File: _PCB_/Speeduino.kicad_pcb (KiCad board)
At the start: 2 copper layers, 100 x 100 mm, 13 parts, among them U1 TC4424AVOA, U2 TC4424AVOA

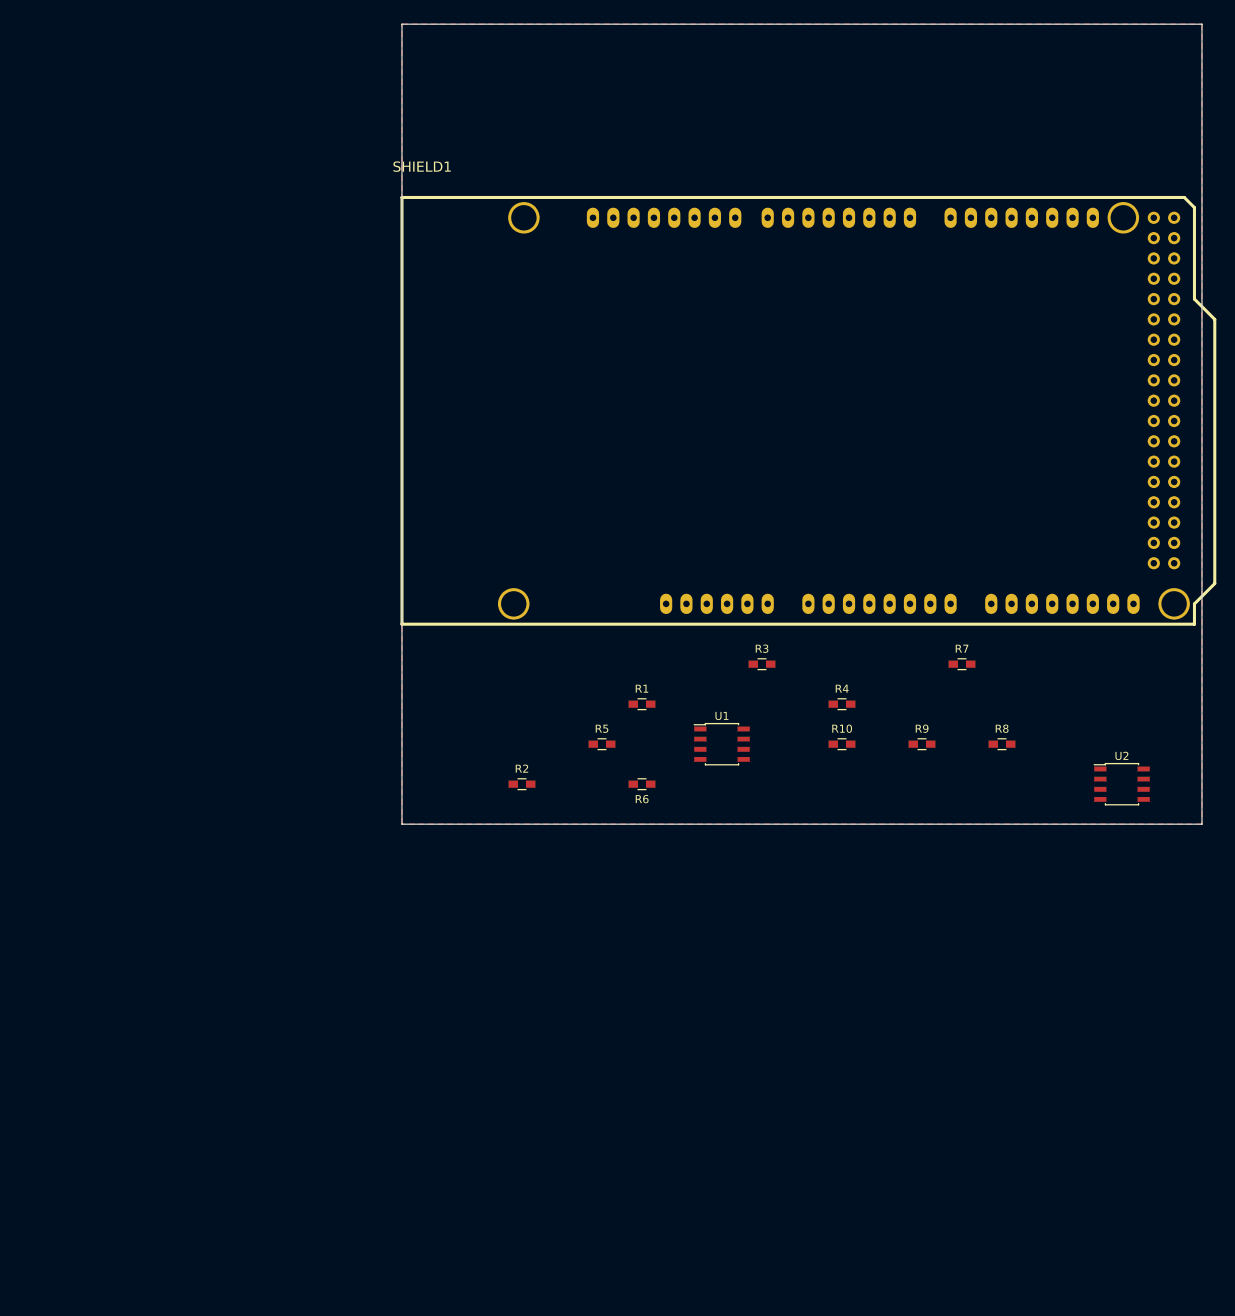
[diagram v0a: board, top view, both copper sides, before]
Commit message: - ajout schematic 4 injecteurs
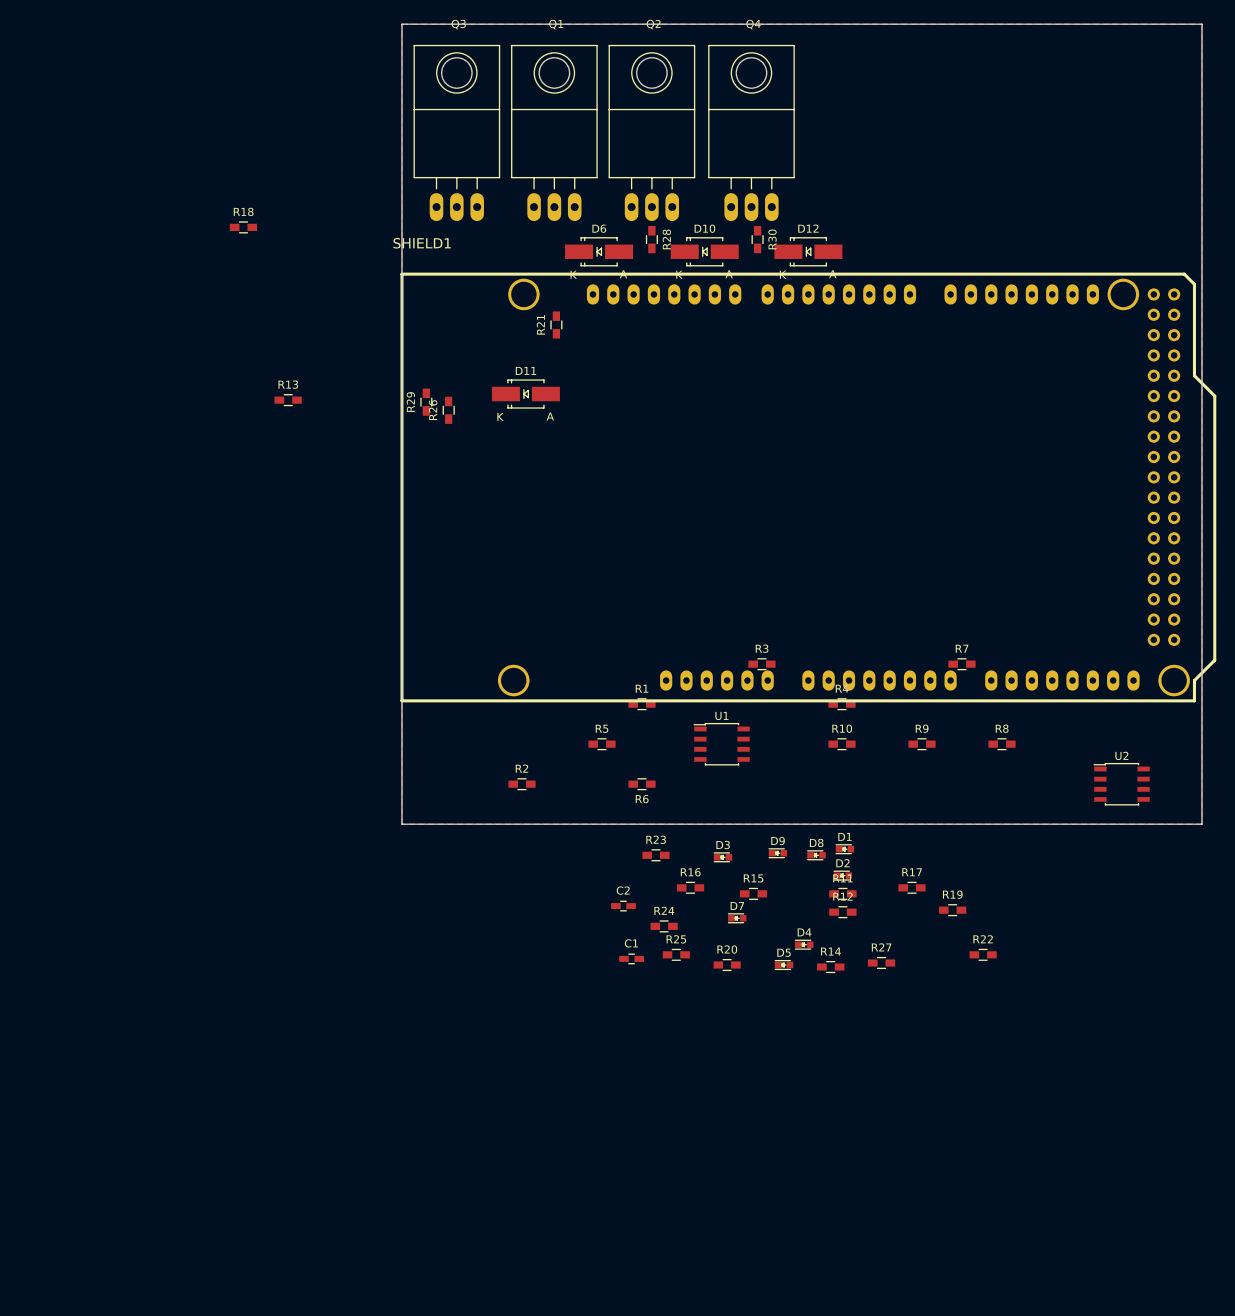
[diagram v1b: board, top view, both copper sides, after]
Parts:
- added C1: C, Speeduino:C_0603_HandSoldering, F.Cu at (108.7, 146.8)
- added C2: C, Speeduino:C_0603_HandSoldering, F.Cu at (107.7, 140.2)
- added D1: LED, Speeduino:LED_0603, F.Cu at (135.4, 133.1)
- added D10: D, Speeduino:SMA_Handsoldering, F.Cu at (117.8, 58.4)
- added D11: D, Speeduino:SMA_Handsoldering, F.Cu at (95.5, 76.2)
- added D12: D, Speeduino:SMA_Handsoldering, F.Cu at (130.8, 58.4)
- added D2: LED, Speeduino:LED_0603, F.Cu at (135.1, 136.4)
- added D3: LED, Speeduino:LED_0603, F.Cu at (120.1, 134.1)
- added D4: LED, Speeduino:LED_0603, F.Cu at (130.3, 145.1)
- added D5: LED, Speeduino:LED_0603, F.Cu at (127.8, 147.6)
- added D6: D, Speeduino:SMA_Handsoldering, F.Cu at (104.6, 58.4)
- added D7: LED, Speeduino:LED_0603, F.Cu at (121.9, 141.8)
- added D8: LED, Speeduino:LED_0603, F.Cu at (131.8, 133.9)
- added D9: LED, Speeduino:LED_0603, F.Cu at (127.0, 133.6)
- added Q1: STP62NS04Z, Speeduino:TO-220_Neutral123_Horizontal_LargePads, F.Cu at (99.0, 52.9)
- added Q2: STP62NS04Z, Speeduino:TO-220_Neutral123_Horizontal_LargePads, F.Cu at (111.2, 52.9)
- added Q3: STP62NS04Z, Speeduino:TO-220_Neutral123_Horizontal_LargePads, F.Cu at (86.9, 52.9)
- added Q4: STP62NS04Z, Speeduino:TO-220_Neutral123_Horizontal_LargePads, F.Cu at (123.7, 52.9)
- added R11: R, Speeduino:R_0603_HandSoldering, F.Cu at (135.1, 138.7)
- added R12: R, Speeduino:R_0603_HandSoldering, F.Cu at (135.1, 141.0)
- added R13: R, Speeduino:R_0603_HandSoldering, F.Cu at (65.8, 77.0)
- added R14: R, Speeduino:R_0603_HandSoldering, F.Cu at (133.6, 147.9)
- added R15: R, Speeduino:R_0603_HandSoldering, F.Cu at (123.9, 138.7)
- added R16: R, Speeduino:R_0603_HandSoldering, F.Cu at (116.1, 137.9)
- added R17: R, Speeduino:R_0603_HandSoldering, F.Cu at (143.8, 137.9)
- added R18: R, Speeduino:R_0603_HandSoldering, F.Cu at (60.2, 55.4)
- added R19: 680, Speeduino:R_0603_HandSoldering, F.Cu at (148.8, 140.7)
- added R20: 100K, Speeduino:R_0603_HandSoldering, F.Cu at (120.6, 147.6)
- added R21: 1K, Speeduino:R_0603_HandSoldering, F.Cu at (99.3, 67.6)
- added R22: 680, Speeduino:R_0603_HandSoldering, F.Cu at (152.6, 146.3)
- added R23: 680, Speeduino:R_0603_HandSoldering, F.Cu at (111.8, 133.9)
- added R24: 680, Speeduino:R_0603_HandSoldering, F.Cu at (112.8, 142.8)
- added R25: 100K, Speeduino:R_0603_HandSoldering, F.Cu at (114.3, 146.3)
- added R26: 100K, Speeduino:R_0603_HandSoldering, F.Cu at (85.8, 78.3)
- added R27: 100K, Speeduino:R_0603_HandSoldering, F.Cu at (139.9, 147.3)
- added R28: 1K, Speeduino:R_0603_HandSoldering, F.Cu at (111.2, 56.9)
- added R29: 1K, Speeduino:R_0603_HandSoldering, F.Cu at (83.0, 77.2)
- added R30: 1K, Speeduino:R_0603_HandSoldering, F.Cu at (124.5, 56.9)
- moved SHIELD1 9.58 mm to (80.0, 114.6)
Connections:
- R6 pad 1: (no net) -> +12V
- U1 pad 5: (no net) -> Net-(R11-Pad2)
- U1 pad 7: (no net) -> Net-(R12-Pad2)
- U2 pad 5: (no net) -> Net-(R15-Pad2)
- U2 pad 7: (no net) -> Net-(R16-Pad2)

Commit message: - ajout BSP149
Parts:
- added Q5: BSP149, Speeduino:SOT-223, F.Cu at (150.0, 45.0)
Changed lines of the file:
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@@
 (kicad_pcb (version 4) (host pcbnew 4.0.0-stable)
   (general
-    (links 70)
-    (no_connects 58)
+    (links 71)
+    (no_connects 59)
     (area 79.924999 29.924999 180.075001 130.075001)
     (thickness 1.6)
@@
     (tracks 0)
     (zones 0)
-    (modules 51)
-    (nets 40)
+    (modules 52)
+    (nets 41)
   )
   (page A4)
@@
   (net 38 INJ1-CPU-D8)
   (net 39 INJ2-CPU-D9)
+  (net 40 "Net-(Q5-Pad2)")
   (net_class Default "Ceci est la Netclass par défaut"
     (clearance 0.2)
@@
     (add_net "Net-(Q3-Pad1)")
     (add_net "Net-(Q4-Pad1)")
+    (add_net "Net-(Q5-Pad2)")
     (add_net "Net-(R1-Pad1)")
     (add_net "Net-(R10-Pad1)")
@@
       (rotate (xyz 0 0 0))
     )
+  )
+  (module Speeduino:SOT-223 (layer F.Cu)
+    (at 150 45)
+    (descr "module CMS SOT223 4 pins")
+    (tags "CMS SOT")
+    (attr smd)
+    (fp_text reference Q5 (at 0 -0.762) (layer F.SilkS)
+      (effects (font (size 1 1) (thickness 0.15)))
+    )
+    (fp_text value BSP149 (at 0 0.762) (layer F.Fab)
+      (effects (font (size 1 1) (thickness 0.15)))
+    )
+    (fp_line (start -3.556 1.524) (end -3.556 4.572) (layer F.SilkS) (width 0.15))
+    (fp_line (start -3.556 4.572) (end 3.556 4.572) (layer F.SilkS) (width 0.15))
+    (fp_line (start 3.556 4.572) (end 3.556 1.524) (layer F.SilkS) (width 0.15))
+    (fp_line (start -3.556 -1.524) (end -3.556 -2.286) (layer F.SilkS) (width 0.15))
+    (fp_line (start -3.556 -2.286) (end -2.032 -4.572) (layer F.SilkS) (width 0.15))
+    (fp_line (start -2.032 -4.572) (end 2.032 -4.572) (layer F.SilkS) (width 0.15))
+    (fp_line (start 2.032 -4.572) (end 3.556 -2.286) (layer F.SilkS) (width 0.15))
+    (fp_line (start 3.556 -2.286) (end 3.556 -1.524) (layer F.SilkS) (width 0.15))
+    (pad 4 smd rect (at 0 -3.302) (size 3.6576 2.032) (layers F.Cu F.Paste F.Mask)
+      (net 40 "Net-(Q5-Pad2)"))
+    (pad 2 smd rect (at 0 3.302) (size 1.016 2.032) (layers F.Cu F.Paste F.Mask)
+      (net 40 "Net-(Q5-Pad2)"))
+    (pad 3 smd rect (at 2.286 3.302) (size 1.016 2.032) (layers F.Cu F.Paste F.Mask))
+    (pad 1 smd rect (at -2.286 3.302) (size 1.016 2.032) (layers F.Cu F.Paste F.Mask))
+    (model TO_SOT_Packages_SMD.3dshapes/SOT-223.wrl
+      (at (xyz 0 0 0))
+      (scale (xyz 0.4 0.4 0.4))
+      (rotate (xyz 0 0 0))
+    )

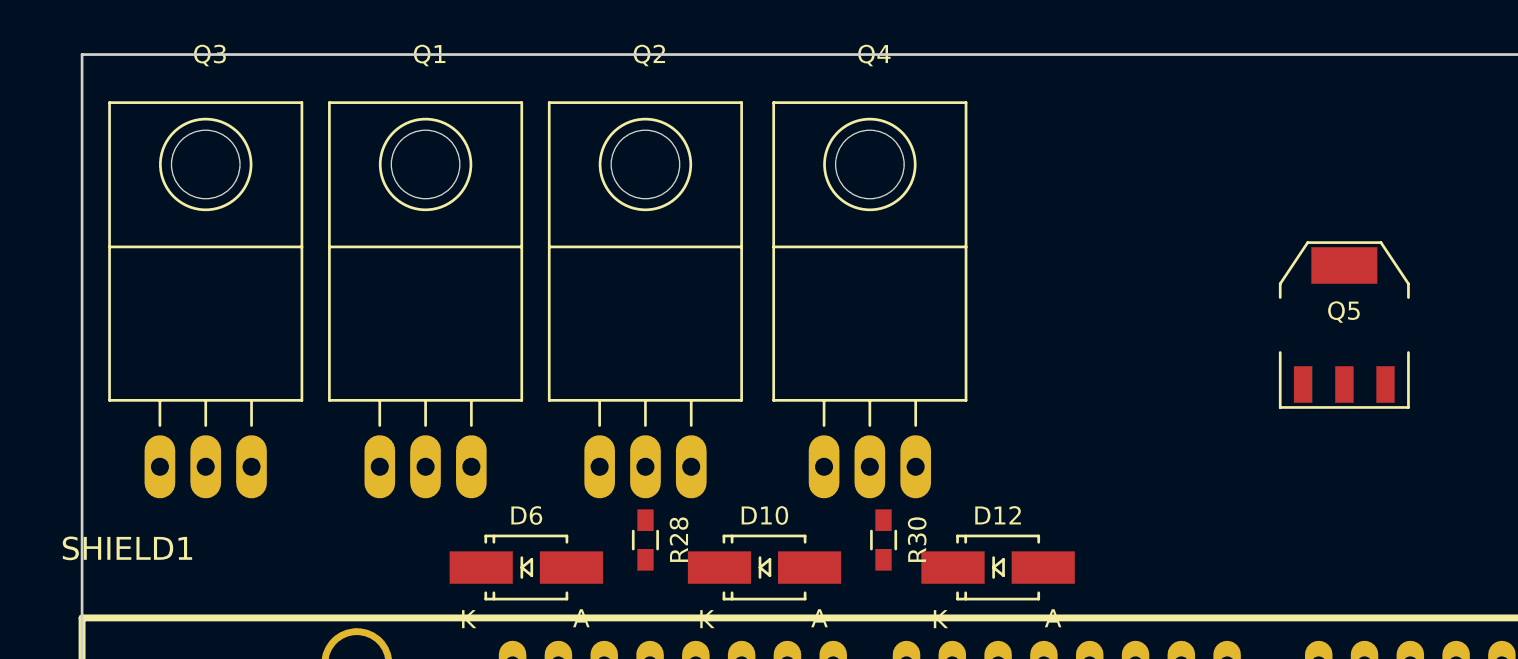
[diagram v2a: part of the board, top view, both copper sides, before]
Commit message: changement de transistor sur les sorties
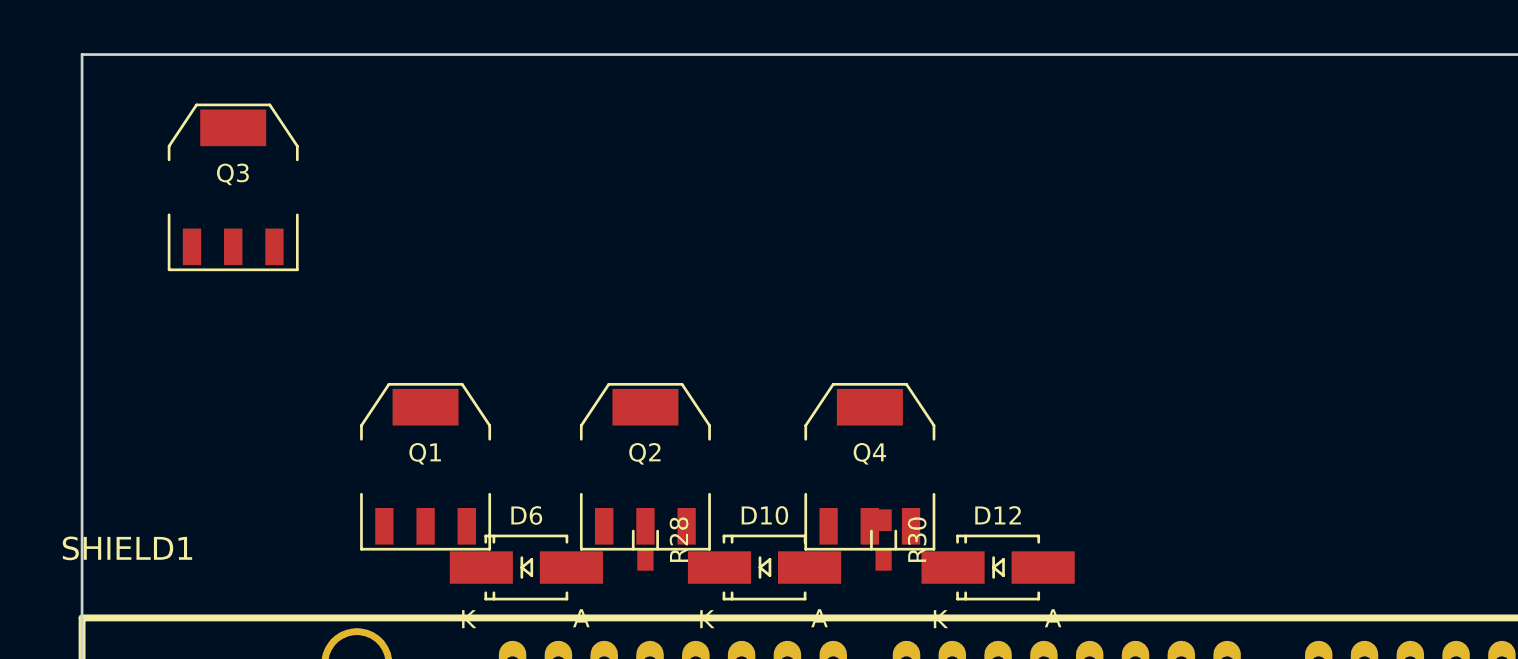
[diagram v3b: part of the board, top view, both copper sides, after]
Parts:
- removed Q5: BSP149, Speeduino:SOT-223
- Q1, Q2, Q3, Q4: value STP62NS04Z -> BSP149; footprint Speeduino:TO-220_Neutral123_Horizontal_LargePads -> Speeduino:SOT-223
- moved Q3 15.6 mm to (88.4, 37.4)
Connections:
- Q3 pad 2: INJ-1-OUT -> INJ-2-OUT
- Q4 pad 2: INJ-2-OUT -> INJ-1-OUT
- R29 pad 1: Net-(Q3-Pad1) -> Net-(Q4-Pad1)
- R30 pad 1: Net-(Q4-Pad1) -> Net-(Q3-Pad1)

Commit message: - modification majeur sur les sortie injecteur . - pas d'étage de puissance sur les sorties injecteurs
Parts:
- removed D10, D11, D12: D, Speeduino:SMA_Handsoldering
- removed D9: LED, Speeduino:LED_0603
- removed Q1, Q2, Q3, Q4: BSP149, Speeduino:SOT-223
- D6: value D -> LED; footprint Speeduino:SMA_Handsoldering -> Speeduino:LED_0603
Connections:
- D5 pad 2: Net-(D5-Pad2) -> INJ3-CPU-D10
- D6 pad 1: INJ-3-OUT -> Net-(D6-Pad1)
- D6 pad 2: Net-(D5-Pad1) -> INJ4-CPU-D11
- D7 pad 1: Net-(D10-Pad2) -> Net-(D7-Pad1)
- D7 pad 2: Net-(D7-Pad2) -> INJ1-CPU-D8
- D8 pad 1: Net-(D11-Pad2) -> Net-(D8-Pad1)
- D8 pad 2: Net-(D8-Pad2) -> INJ2-CPU-D9
- R19 pad 1: Net-(D5-Pad2) -> GND
- R19 pad 2: +12V -> Net-(D5-Pad1)
- R21 pad 1: Net-(Q1-Pad1) -> (no net)
- R22 pad 1: Net-(D7-Pad2) -> GND
- R22 pad 2: +12V -> Net-(D6-Pad1)
- R23 pad 1: Net-(D8-Pad2) -> GND
- R23 pad 2: +12V -> Net-(D7-Pad1)
- R24 pad 1: Net-(D9-Pad2) -> GND
- R24 pad 2: +12V -> Net-(D8-Pad1)
- R28 pad 1: Net-(Q2-Pad1) -> (no net)
- R29 pad 1: Net-(Q4-Pad1) -> (no net)
- R30 pad 1: Net-(Q3-Pad1) -> (no net)
- R6 pad 1: +12V -> (no net)
